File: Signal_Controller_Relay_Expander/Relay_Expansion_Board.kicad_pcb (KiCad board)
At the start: 2 copper layers, 60 x 60 mm, 22 parts, among them J1 CONN_01X05, J2 CONN_01X02, J3 CONN_01X02, Q1 2N7002P,215, Q2 2N7002P,215, Q3 2N7002P,215

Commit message: I looked at it (minor tweaks)
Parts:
- R1: value R -> 3.3K
- moved ? 0.16 mm to (182.0, 119.5)
- moved ? 0.13 mm to (129.0, 119.5)
- moved ? 0.13 mm to (182.0, 66.5)
- moved ? 0.08 mm to (129.0, 66.5)
- renumbered REF** to ?

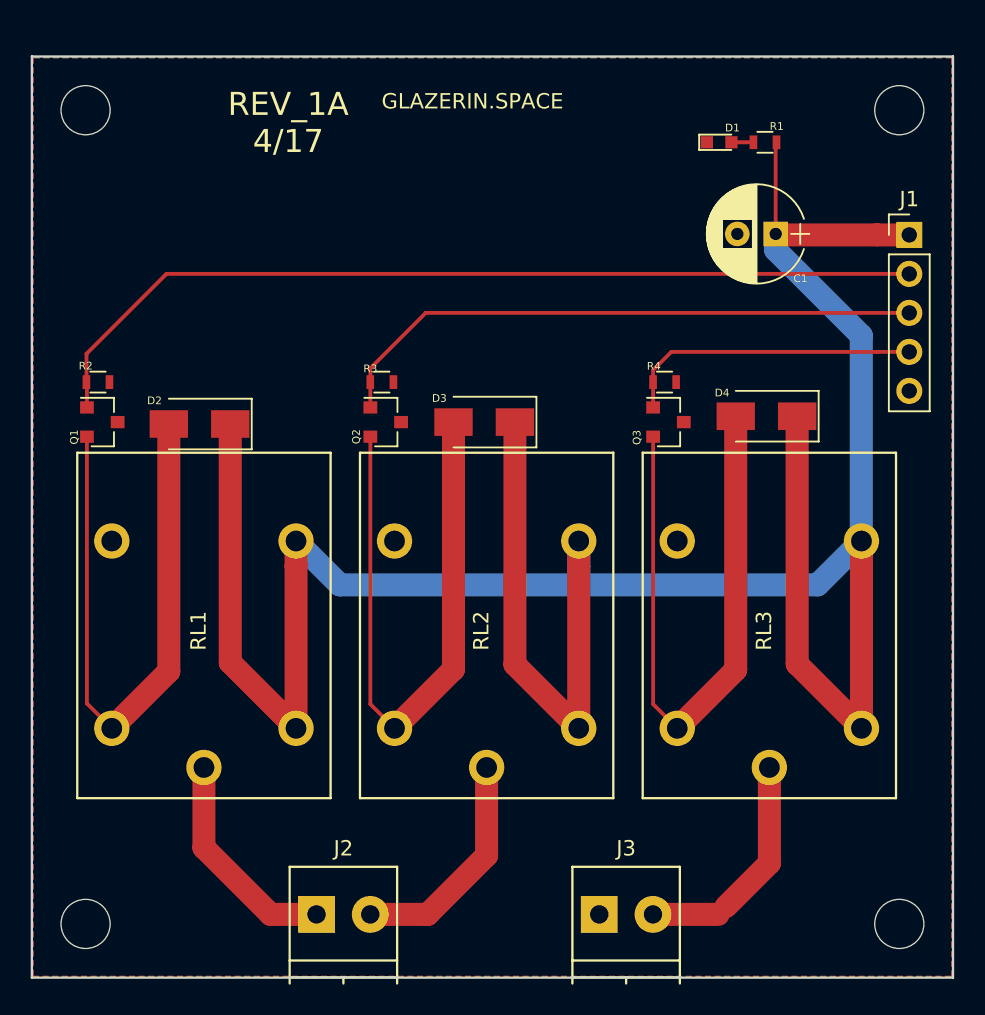
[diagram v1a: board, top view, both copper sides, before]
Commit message: moved relays and connector to line up with controller board
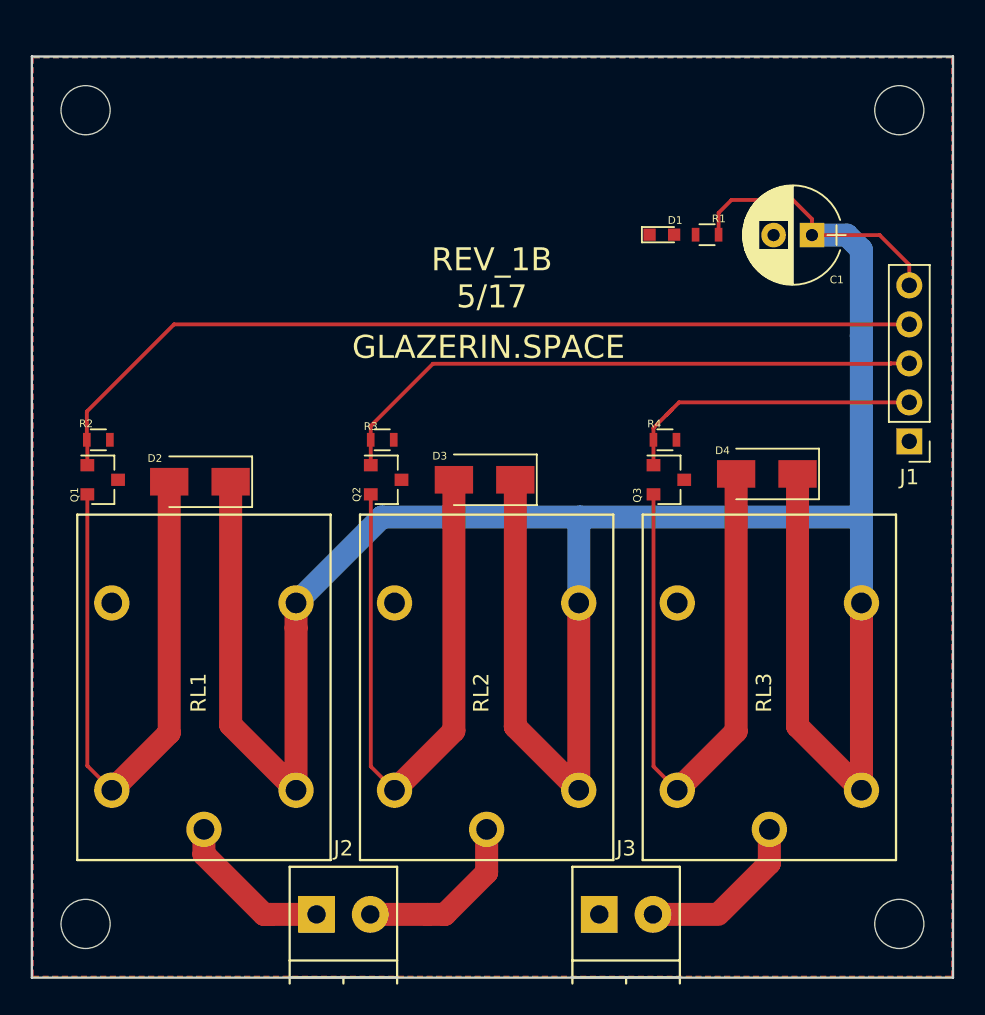
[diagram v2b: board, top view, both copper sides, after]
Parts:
- R1: value 3.3K -> R
- moved J1 13.4 mm to (182.6, 88.1), turned to 180 degrees
- moved R1 7.10 mm to (169.5, 74.6)
- moved D1 7.08 mm to (166.5, 74.6)
- moved RL1 4.03 mm to (142.7, 110.8)
- moved RL2 4.03 mm to (161.1, 110.8)
- moved RL3 4.03 mm to (179.5, 110.8)
- moved D2 3.76 mm to (136.4, 90.7)
- moved R2 3.76 mm to (129.8, 88.0)
- moved R3 3.76 mm to (148.3, 88.0)
- moved R4 3.76 mm to (166.7, 88.0)
- moved D3 3.76 mm to (155.0, 90.6)
- moved D4 3.76 mm to (173.3, 90.2)
- moved Q1 3.76 mm to (130.1, 90.6)
- moved Q2 3.76 mm to (148.6, 90.6)
- moved Q3 3.76 mm to (167.0, 90.6)
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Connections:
- J1 pad 1: +12V -> GND
- J1 pad 2: /RELAY_4 -> /RELAY_6
- J1 pad 4: /RELAY_6 -> /RELAY_4
- J1 pad 5: GND -> +12V
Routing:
- net +12V: track 181.0 -> 192.2 mm
- net /COIL_2A: track 14.4 -> 10.6 mm
- net /BULB_2: track 15.3 -> 11.7 mm
- net /COIL_2B: track 14.9 -> 11.5 mm
- net Net-(D1-Pad2): track 1.43 -> 0.00 mm
- net /RELAY_6: track 19.6 -> 20.3 mm
- net Net-(D3-Pad2): track 41.2 -> 41.7 mm
- net Net-(D4-Pad2): track 41.6 -> 42.1 mm
- net Net-(D2-Pad2): track 41.0 -> 41.6 mm
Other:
- board text added: "REV_1B 5/17"
- board text removed: "REV_1A 4/17"
